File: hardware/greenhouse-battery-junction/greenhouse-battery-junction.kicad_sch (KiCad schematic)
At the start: 23 parts, among them J1 Conn_01x10_Female, J10 Conn_01x03_Female, J11 Screw_Terminal_01x02, J12 Conn_01x04_Male, J2 Conn_01x03_Female

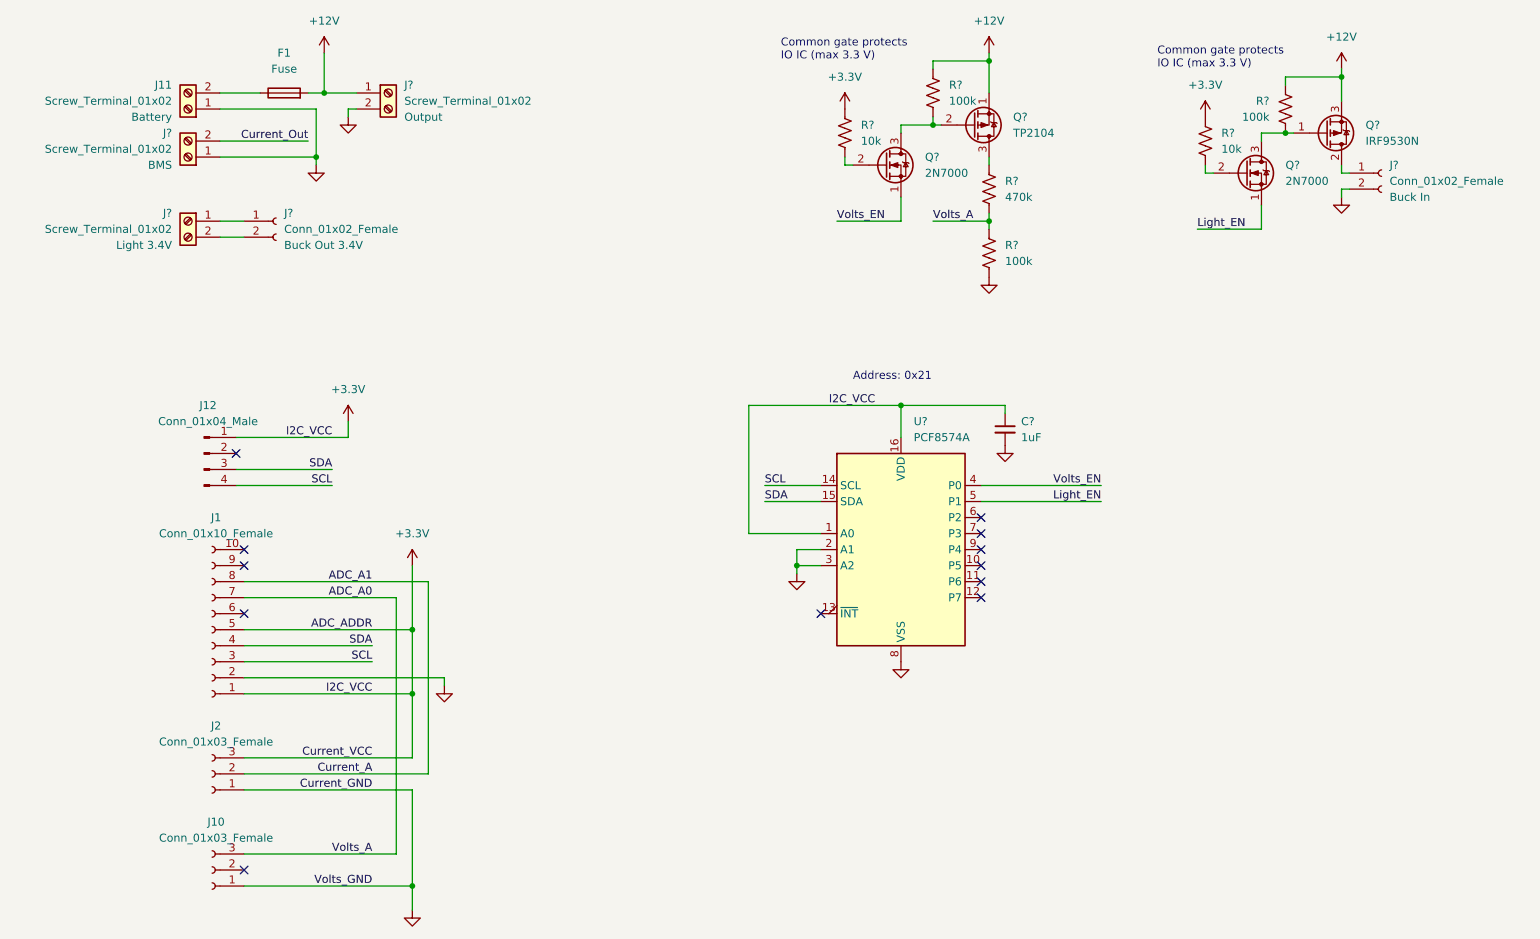
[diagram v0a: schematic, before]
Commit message: Hardware R4 (KiCAD 7) (#310)
* First pass at R4

* Optimized power use and moved beeper

* Separate battery and PV voltage sensors

* Tweak traces

* Replace diode with back-to-back FET

* Add notes to schematic

* Remove IO switch for voltage sensor

Also changed ADS range to 2V

* Improved GND loop for battery ADC

* Add note to schematic

* Updated ESP32 footprint

* Increase weather report timeout

* Turn on PSU and wait

Maybe this will allow caps to charge first, which could solve #306

* Add trace for switch delay

* WIP: Add MPPT module

And reorganised board to fit
Traces to do

* Made prototype footprints clearer

* Connected hand side of PCB

* Extended I2C ADC retry

I2C connection seems to sometimes recover after 6 seconds, but it's unreliable (can stay failed after 20 seconds)

* Extra logging for ADC busy/retry

* Shortened ADC retry

* LoRa enable macro + extra logs

* Refactored mapFloat

* Update platformio.ini

* Fixed DRC errors

* Moved MCU and LoRa module

PCF8574's no longer under MCU

* Fixed silk screen and power planes

* Increased ADC voltage rage

* Remove I2C GND connection

Use main GND connection instead

* Add TODOs

* Changed to PNP for PSU/batt

Also:
- Swapped MCU and LoRa module
- Add flyback diodes (power out + relay)
- Add +12V (for external USB, etc)

* Repositioned flyback diodes

* Fixed PNP connections

* Add TODO (MCU type/IOs)

* Fixed #309

* Fixed: case fan only changes on power switch

* Fixed MCU courtyard

* Fixed fuse holder, add KK 396 models

* Tweaked traces and vias

Also updated some footprints

* Fixed relay driver, fine tuned traces

* Pin libs

* Tweak tracks

* Delete greenhouse-control-unit.xml

* Switched to RFM69 (SMD)

Also moved MCU, and updated some 3D models, extra SS for VAC warning, current info for KK connectors

* Update .gitignore

* Rename and update BOM

* Update greenhouse-control-unit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
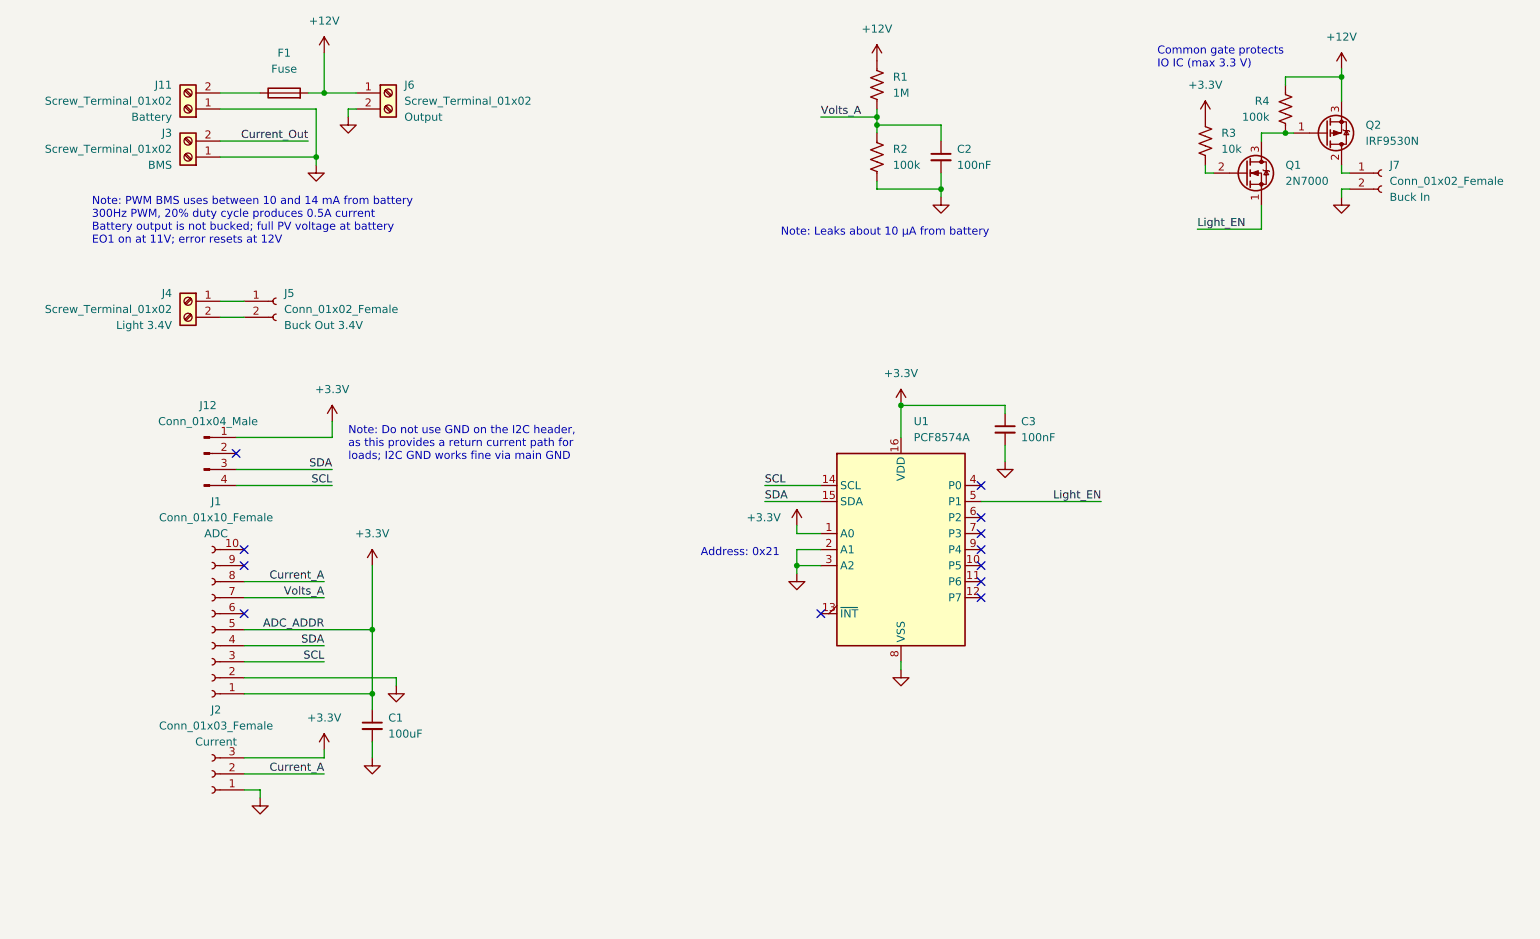
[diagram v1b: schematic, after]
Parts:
- removed J10: Conn_01x03_Female, Connector_PinHeader_2.54mm:PinHeader_1x03_P2.54mm_Vertical, symbol Connector:Conn_01x03_Female
- removed Q?: TP2104, Package_TO_SOT_THT:TO-92_Inline, symbol Device:Q_PMOS_SGD
- removed Q?: 2N7000, Package_TO_SOT_THT:TO-92_Inline, symbol Transistor_FET:2N7000
- removed R?: 10k, symbol Device:R_US
- removed R?: 100k, symbol Device:R_US
- added C1: 100uF, symbol Device:C_Small
- added C2: 100nF, symbol Device:C_Small
- C3: renamed from C?; value 1uF -> 100nF
- J1: Module (none) -> ADC
- J2: Module (none) -> Current
- R1: renamed from R?; value 470k -> 1M
- gave numbers to parts that had none: 11
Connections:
- net +12V: now also R1.1
- net +3V3: now also C1.1
- net GND: now also C1.2, C2.2
- net ADC_A0 renamed Volts_A
- net Volts_A: now also C2.1
- net ADC_A1 renamed Current_A
- net Volts_EN: no longer names the net of U1.4 (P0)
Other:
- note added: "Note: Do not use GND on the I2C header, as this provides a return current path for loads; I2C GND works fine via main GND"
- note added: "Note: Leaks about 10 μA from battery"
- note added: "Note: PWM BMS uses between 10 and 14 mA from battery 300Hz PWM, 20% duty cycle produces 0.5A current Battery output is not bucked; full PV voltage at battery EO1 on at 11V; error resets at 12V"
- moved on the sheet: J4, J5, R1, R2
